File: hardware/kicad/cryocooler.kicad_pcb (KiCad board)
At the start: 4 copper layers, 130 x 100 mm, 208 parts, among them J1 USB_C, J10 RTD PT1000 4-wire, J11 AMP OUT (+ / -), J12 CRYOCOOLER (+ / -), J2 12V IN, J3 FAN (4-pin PWM), J4 PUMP (4-pin PWM), J5 ALPHACOOL ES FLOW (3-pin), J6 ALPHACOOL ES NTC 10k, J7 PANEL BUTTON, J8 AMP REM / GND, J9 AMP SIGNAL IN / GND, Q1 IRF4905S, Q2 BSS138, Q3 BSS138, Q4 BSS138, Q5 BSS138, Q6 BSS84, SW1 RESET, SW2 BOOT, SW3 POWER, U1 ESP32-S3-WROOM-2-N32R16V, U10 EMC2303-x-KP, U11 LTC2954CTS8-2, U12 LM4040DBZ-5, U13 CL25N8-G, U14 ADS122C04IPWR, U15 AP63205WU-7, U16 LD1117S33TR, U17 ISO7741DW, U18 ACS37800KMACTR-030B3-SPI, U19 LSM6DSOXTR, U2 USBLC6-2SC6, U20 ADP5071AREZ, U21 ADP7142AUJZ, U22 ADP7182AUJZ, U23 INA237AIDGSR, U24 74AHCT1G125, U3 SG-8002CA-PH 25MHz, U4 AD9833BRMZ, U5 OPA1656ID, U6 AD633JRZ-R7, U7 MCP4921-E/SN, U8 LM4040DBZ-2.5, U9 OPA188ID

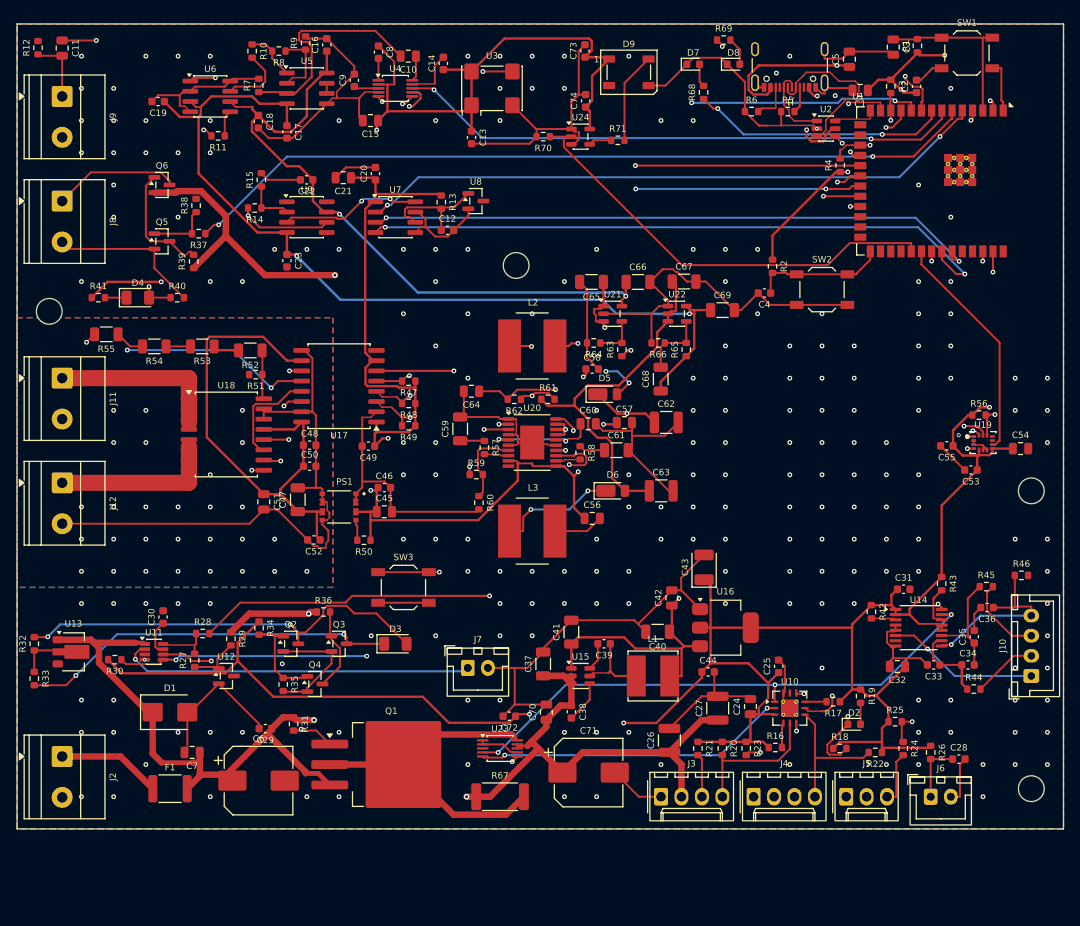
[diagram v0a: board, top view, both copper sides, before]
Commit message: KiCad PCB: regenerate and route for the new parts (DRC 0 errors, 0 unconnected)
- Places the INA239 LEDs and filter, the compressor relay driver, the
  SC18IS604 and its buffer, and about 40 test points; test points and the
  debug LEDs are placed beside a pad on their net.
- gen_pcb.py fixes: escape stubs now sample the whole stub and ignore only
  the pad's own tracks (diagonal-track bounding boxes hid real obstacles);
  isolated-side passives are derived from nets instead of fixed refs; ground
  pads boxed in by tracks get an escape via; locked 0.35 mm via-in-pad on the
  fine-pitch ground pads of U19, U23 and U4 before routing.
- tools/link_usb_vbus.py joins the USB-C VBUS pad pairs after routing.
- cryocooler.kicad_pro: net classes plus 0.35 mm via / 0.075 mm annular ring /
  0.2 mm drill limits for the via-in-pad (check the fab's minimums).

All 807 pad nets match the schematic netlist; only silkscreen warnings remain.

Co-Authored-By: Claude Sonnet 5.5 <noreply@anthropic.com>
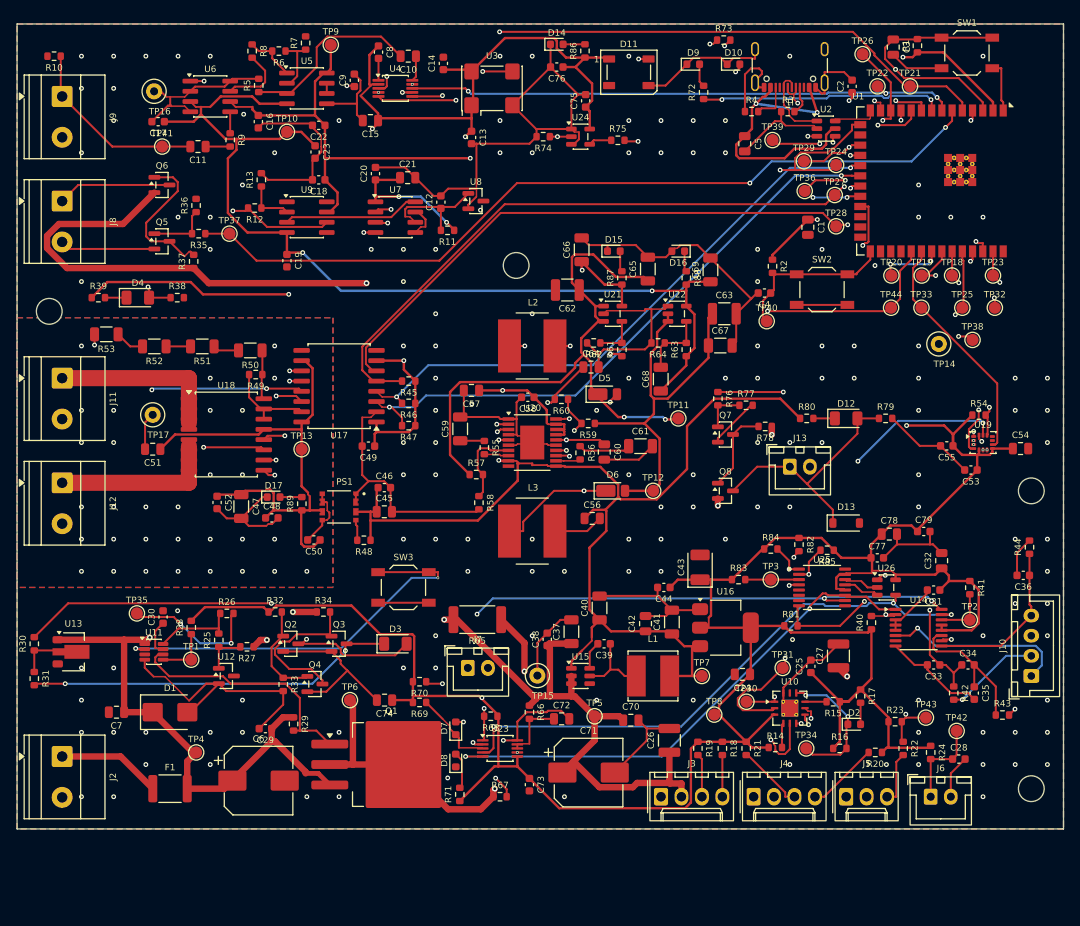
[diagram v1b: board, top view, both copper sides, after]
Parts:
- added C75: 100nF, C_0603_1608Metric, F.Cu at (70.6, 9.55)
- added C76: 100nF, C_0603_1608Metric, F.Cu at (67.0, 5.35)
- added C77: 100nF, C_0603_1608Metric, F.Cu at (106.9, 66.3)
- added C78: 1uF, C_0805_2012Metric, F.Cu at (108.4, 63.4)
- added C79: 100nF, C_0603_1608Metric, F.Cu at (112.6, 63.0)
- added D10: FAULT (red), LED_0603_1608Metric, F.Cu at (89.0, 5.00)
- added D11: WS2812B, LED_WS2812B_PLCC4_5.0x5.0mm_P3.2mm, F.Cu at (76.0, 6.00)
- added D12: RED/GREEN, LED_1206_3216Metric, F.Cu at (103.0, 49.0)
- added D13: 1N4148W, D_SOD-123, F.Cu at (103.0, 62.0)
- added D14: 5V (yellow), LED_0603_1608Metric, F.Cu at (67.0, 2.52)
- added D15: +15V (white), LED_0603_1608Metric, F.Cu at (74.1, 28.2)
- added D16: -15V (white), LED_0603_1608Metric, F.Cu at (82.1, 28.2)
- added D17: ISO 3V3 (green), LED_0603_1608Metric, F.Cu at (31.9, 58.8)
- added J13: COMPRESSOR RELAY / GND, JST_XH_B2B-XH-A_1x02_P2.50mm_Vertical, F.Cu at (96.0, 55.0)
- added Q7: BSS138, SOT-23, F.Cu at (88.0, 51.0)
- added Q8: BSS84, SOT-23, F.Cu at (88.0, 58.0)
- added R72: 470, R_0603_1608Metric, F.Cu at (85.3, 8.50)
- added R73: 470, R_0603_1608Metric, F.Cu at (87.8, 2.00)
- added R74: 10k, R_0603_1608Metric, F.Cu at (65.4, 14.0)
- added R75: 330, R_0603_1608Metric, F.Cu at (74.6, 14.4)
- added R76: 1k, R_0603_1608Metric, F.Cu at (87.1, 46.5)
- added R77: 100k, R_0603_1608Metric, F.Cu at (90.6, 47.4)
- added R78: 100k, R_0603_1608Metric, F.Cu at (92.9, 50.0)
- added R79: 1k, R_0603_1608Metric, F.Cu at (107.9, 49.0)
- added R80: 2.2k, R_0603_1608Metric, F.Cu at (98.1, 49.0)
- added R81: 10k, R_0603_1608Metric, F.Cu at (96.1, 74.8)
- added R82: 10k, R_0603_1608Metric, F.Cu at (97.1, 64.7)
- added R83: 10k, R_0603_1608Metric, F.Cu at (89.6, 69.0)
- added R84: 4.7k, R_0603_1608Metric, F.Cu at (93.6, 65.2)
- added R85: 4.7k, R_0603_1608Metric, F.Cu at (100.6, 65.4)
- added R86: 1k, R_0603_1608Metric, F.Cu at (70.5, 3.35)
- added R87: 4.7k, R_0603_1608Metric, F.Cu at (75.1, 31.6)
- added R88: 4.7k, R_0603_1608Metric, F.Cu at (83.1, 31.6)
- added R89: 1k, R_0603_1608Metric, F.Cu at (35.4, 59.6)
- added TP1: LTC2954_INT, TestPoint_Pad_D1.5mm, F.Cu at (21.6, 79.0)
- added TP10: -15V, TestPoint_Pad_D1.5mm, F.Cu at (33.5, 13.4)
- added TP11: +16V5, TestPoint_Pad_D1.5mm, F.Cu at (82.2, 49.0)
- added TP12: -16V5, TestPoint_Pad_D1.5mm, F.Cu at (79.0, 58.0)
- added TP13: ISO_3V3, TestPoint_Pad_D1.5mm, F.Cu at (35.4, 52.8)
- added TP14: GND, TestPoint_Loop_D2.50mm_Drill1.0mm, F.Cu at (114.5, 39.8)
- added TP15: GND, TestPoint_Loop_D2.50mm_Drill1.0mm, F.Cu at (64.6, 81.0)
- added TP16: GND, TestPoint_Loop_D2.50mm_Drill1.0mm, F.Cu at (17.0, 8.37)
- added TP17: ISO_GND, TestPoint_Loop_D2.50mm_Drill1.0mm, F.Cu at (16.9, 48.6)
- added TP18: SPI_SCK, TestPoint_Pad_D1.5mm, F.Cu at (116.2, 31.2)
- added TP19: SPI_MOSI, TestPoint_Pad_D1.5mm, F.Cu at (112.4, 31.2)
- added TP2: ADS1220_DRDY, TestPoint_Pad_D1.5mm, F.Cu at (118.4, 74.0)
- added TP20: SPI_MISO, TestPoint_Pad_D1.5mm, F.Cu at (108.6, 31.2)
- added TP21: MCP4921_CS, TestPoint_Pad_D1.5mm, F.Cu at (110.9, 7.75)
- added TP22: AD9833_FSYNC, TestPoint_Pad_D1.5mm, F.Cu at (106.9, 7.75)
- added TP23: IMU_CS, TestPoint_Pad_D1.5mm, F.Cu at (121.2, 31.2)
- added TP24: INA239_CS, TestPoint_Pad_D1.5mm, F.Cu at (101.8, 17.5)
- added TP25: ADS1220_CS, TestPoint_Pad_D1.5mm, F.Cu at (117.4, 35.2)
- added TP26: BRIDGE_CS, TestPoint_Pad_D1.5mm, F.Cu at (105.0, 3.75)
- added TP27: ACS_CS, TestPoint_Pad_D1.5mm, F.Cu at (101.6, 21.2)
- added TP28: ACS_MISO, TestPoint_Pad_D1.5mm, F.Cu at (101.8, 25.1)
- added TP29: BRIDGE_RESET, TestPoint_Pad_D1.5mm, F.Cu at (97.8, 17.1)
- added TP3: BRIDGE_INT, TestPoint_Pad_D1.5mm, F.Cu at (93.6, 69.0)
- added TP30: SDA, TestPoint_Pad_D1.5mm, F.Cu at (90.6, 84.2)
- added TP31: SCL, TestPoint_Pad_D1.5mm, F.Cu at (95.1, 80.0)
- added TP32: IMU_INT1, TestPoint_Pad_D1.5mm, F.Cu at (121.5, 35.2)
- added TP33: IMU_INT2, TestPoint_Pad_D1.5mm, F.Cu at (112.3, 35.2)
- added TP34: FAN_ALERT, TestPoint_Pad_D1.5mm, F.Cu at (98.0, 90.0)
- added TP35: PWR_KILL, TestPoint_Pad_D1.5mm, F.Cu at (14.9, 73.2)
- added TP36: COMP_RELAY_EN, TestPoint_Pad_D1.5mm, F.Cu at (97.8, 20.8)
- added TP37: AMP_REM_EN, TestPoint_Pad_D1.5mm, F.Cu at (26.4, 26.1)
- added TP38: UART0_TX, TestPoint_Pad_D1.5mm, F.Cu at (118.7, 39.2)
- added TP39: ESP_EN, TestPoint_Pad_D1.5mm, F.Cu at (93.8, 14.4)
- added TP4: VIN, TestPoint_Pad_D1.5mm, F.Cu at (22.2, 90.5)
- added TP40: ESP_BOOT, TestPoint_Pad_D1.5mm, F.Cu at (93.1, 36.9)
- added TP41: SIG_SINE, TestPoint_Pad_D1.5mm, F.Cu at (18.0, 15.2)
- added TP42: NTC_ADC, TestPoint_Pad_D1.5mm, F.Cu at (116.7, 87.8)
- added TP43: FLOW_TACH, TestPoint_Pad_D1.5mm, F.Cu at (112.9, 86.2)
- added TP44: STATUS_RGB, TestPoint_Pad_D1.5mm, F.Cu at (108.6, 35.2)
- added TP5: +12V, TestPoint_Pad_D1.5mm, F.Cu at (71.8, 86.0)
- added TP6: VSW, TestPoint_Pad_D1.5mm, F.Cu at (41.4, 84.0)
- added TP7: +5V, TestPoint_Pad_D1.5mm, F.Cu at (85.1, 81.0)
- added TP8: +3V3, TestPoint_Pad_D1.5mm, F.Cu at (86.6, 85.8)
- added TP9: +15V, TestPoint_Pad_D1.5mm, F.Cu at (39.0, 2.60)
- added U25: SC18IS604PW, TSSOP-16_4.4x5mm_P0.65mm, F.Cu at (100.0, 70.0)
- added U26: 74LVC1G125, SOT-23-5, F.Cu at (108.0, 70.0)
- C72: value 100nF -> 470nF; footprint C_0603_1608Metric -> C_0805_2012Metric
- C74: value 100nF -> 1uF; footprint C_0603_1608Metric -> C_0805_2012Metric
- D7: value READY (green) -> ALERT (red)
- D8: value FAULT (red) -> PWR (green)
- D9: value WS2812B -> READY (green); footprint LED_WS2812B_PLCC4_5.0x5.0mm_P3.2mm -> LED_0603_1608Metric
- R10: value 100 -> 100k
- R11: value 100 -> 6.8k
- R12: value 100k -> 30k
- R13: value 6.8k -> 10k
- R14: value 30k -> 33k
- R15: value 10k -> 4.7k
- R16: value 33k -> 10k
- R17: value 4.7k -> 1k
- R19: value 1k -> 4.7k
- R22, R42, R43, R70: value 10k -> 1k
- R23: value 4.7k -> 10k
- R24, R40, R45: value 1k -> 10k
- R25: value 10k -> 220k
- R27: value 220k -> 82k
- R29: value 82k -> 100k
- R3, R4: value 4.7k -> 5.1k
- R30: value 10k -> 330
- R31: value 100k -> 330
- R32: value 330 -> 10k
- R33: value 330 -> 100k
- R34, R48: value 10k -> 100k
- R35, R38: value 100k -> 1k
- R37: value 1k -> 100k
- R39: value 100k -> 2.2k
- R41: value 2.2k -> 10k
- R44: value 1k -> 3.9k
- R46: value 3.9k -> 10k
- R49: value 10k -> 4.02k
- R5: value 5.1k -> 100k
- R50: value 100k -> 1M; footprint R_0603_1608Metric -> R_1206_3216Metric
- R51: value 4.02k -> 1M; footprint R_0603_1608Metric -> R_1206_3216Metric
- R54: value 1M -> 10k; footprint R_1206_3216Metric -> R_0603_1608Metric
- R55: value 1M -> 5.6k; footprint R_1206_3216Metric -> R_0603_1608Metric
- R56: value 10k -> 12k
- R57: value 5.6k -> 2.67M
- R58: value 12k -> 137k
- R59: value 2.67M -> 2.55M
- R6: value 5.1k -> 51k
- R60: value 137k -> 118k
- R61: value 2.55M -> 115k
- R62: value 118k -> 10k
- R63: value 115k -> 113k
- R65: value 113k -> 15m; footprint R_0603_1608Metric -> R_2512_6332Metric
- R66: value 10k -> 49.9
- R67: value 15m -> 49.9; footprint R_2512_6332Metric -> R_0603_1608Metric
- R68, R69: value 470 -> 10k
- R7: value 100k -> 3.3k
- R71: value 330 -> 470
- R8: value 51k -> 100
- R9: value 3.3k -> 100
- U14: value ADS122C04IPWR -> ADS1220IPW
- U23: value INA237AIDGSR -> INA239AIDGSR
- moved R41 114.1 mm to (118.4, 70.0), turned to -90 degrees
- moved R54 102.8 mm to (119.5, 48.6), turned to 0 degrees
- moved R15 96.2 mm to (101.4, 84.2), turned to 180 degrees
- moved R40 95.2 mm to (106.1, 74.4), turned to 90 degrees
- moved R14 93.1 mm to (94.2, 89.9), turned to 0 degrees
- moved D8 93.1 mm to (54.5, 91.5), turned to 90 degrees
- moved C73 91.4 mm to (63.6, 94.5), turned to -90 degrees
- moved R69 90.5 mm to (50.0, 84.3), turned to 180 degrees
- moved R26 89.1 mm to (26.1, 73.2), turned to 0 degrees
- moved D7 87.6 mm to (54.5, 87.5), turned to 90 degrees
- moved R25 84.6 mm to (25.1, 76.5), turned to 90 degrees
- moved R71 83.6 mm to (55.0, 95.7), turned to 90 degrees
- moved R68 81.9 mm to (58.9, 86.0), turned to 180 degrees
- moved R46 79.1 mm to (48.6, 47.1), turned to 180 degrees
- moved C74 78.5 mm to (45.6, 84.0), turned to 180 degrees
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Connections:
- net /Amp Current/ISO_CS renamed Net-(U17-OUTC)
- net /Amp Current/ISO_MISO renamed Net-(U17-IND)
- net /Amp Current/ISO_MOSI renamed Net-(U17-OUTA)
- net /Amp Current/ISO_SCK renamed Net-(U17-OUTB)
- net Net-(U1-EN) renamed ESP_EN
- net Net-(U1-IO0) renamed ESP_BOOT
- C34 pad 2: Net-(U14-AIN0) -> Net-(U14-AIN0/REFP1)
- C35 pad 1: Net-(U14-AIN0) -> Net-(U14-AIN0/REFP1)
- C72 pad 1: +3V3 -> Net-(U23-IN-)
- C72 pad 2: GND -> Net-(U23-IN+)
- C73 pad 1: +5V -> +3V3
- C74 pad 1: +5V -> +3V3
- D7 pad 1: GND -> Net-(D7-K)
- D9 pad 1: +5V -> GND
- D9 pad 2: unconnected-(D9-DOUT-Pad2) -> Net-(D9-A)
- R10 pad 1: Net-(R10-Pad1) -> SIG_SINE
- R10 pad 2: Net-(U6-X1) -> GND
- R11 pad 1: Net-(U6-W) -> +3V3
- R11 pad 2: Net-(C11-Pad1) -> Net-(U7-Vref)
- R12 pad 1: SIG_SINE -> Net-(U9--)
- R12 pad 2: GND -> Net-(U6-Y1)
- R13 pad 1: +3V3 -> Net-(U9--)
- R13 pad 2: Net-(U7-Vref) -> GND
- R14 pad 1: Net-(U9--) -> +3V3
- R14 pad 2: Net-(U6-Y1) -> Net-(U10-ADDR_SEL)
- R15 pad 1: Net-(U9--) -> +3V3
- R15 pad 2: GND -> Net-(U10-CLK)
- R16 pad 2: Net-(U10-ADDR_SEL) -> FAN_ALERT
- R17 pad 2: Net-(U10-CLK) -> Net-(D2-A)
- R18 pad 2: FAN_ALERT -> Net-(J3-Pin_4)
- R19 pad 2: Net-(D2-A) -> Net-(J3-Pin_3)
- R20 pad 2: Net-(J3-Pin_4) -> Net-(J4-Pin_4)
- R21 pad 2: Net-(J3-Pin_3) -> Net-(J4-Pin_3)
- R22 pad 1: +3V3 -> FLOW_TACH
- R22 pad 2: Net-(J4-Pin_4) -> Net-(J5-Pin_3)
- R23 pad 2: Net-(J4-Pin_3) -> FLOW_TACH
- R24 pad 1: FLOW_TACH -> +3V3
- R24 pad 2: Net-(J5-Pin_3) -> NTC_ADC
- R25 pad 1: +3V3 -> Net-(U12-K)
- R25 pad 2: FLOW_TACH -> Net-(U11-~{KILL})
- R26 pad 1: +3V3 -> Net-(U11-~{KILL})
- R26 pad 2: NTC_ADC -> PWR_KILL
- R27 pad 1: Net-(U12-K) -> VIN
- R27 pad 2: Net-(U11-~{KILL}) -> Net-(U12-K)
- R28 pad 1: Net-(U11-~{KILL}) -> Net-(U11-~{INT})
- R28 pad 2: PWR_KILL -> +3V3
- R29 pad 2: Net-(U12-K) -> Net-(Q1-G)
- R3 pad 1: +3V3 -> GND
- R3 pad 2: SDA -> Net-(J1-CC1)
- R30 pad 1: PWR_INT -> Net-(U13-VB)
- R30 pad 2: +3V3 -> Net-(D3-AK)
- R31 pad 1: VIN -> Net-(U13-VB)
- R31 pad 2: Net-(Q1-G) -> Net-(D3-KA)
- R32 pad 1: Net-(U13-VB) -> +3V3
- R32 pad 2: Net-(D3-AK) -> Net-(Q2-G)
- R33 pad 1: Net-(U13-VB) -> Net-(Q2-G)
- R33 pad 2: Net-(D3-KA) -> GND
- R34 pad 1: +3V3 -> VIN
- R34 pad 2: Net-(Q2-G) -> Net-(Q3-G)
- R35 pad 1: Net-(Q2-G) -> AMP_REM_EN
- R35 pad 2: GND -> Net-(Q5-G)
- R36 pad 1: VIN -> Net-(Q5-G)
- R36 pad 2: Net-(Q3-G) -> GND
- R37 pad 1: AMP_REM_EN -> +12V
- R37 pad 2: Net-(Q5-G) -> Net-(Q5-D)
- R38 pad 1: Net-(Q5-G) -> /Amp Control/AMP_REM
- R39 pad 1: +12V -> +5V
- R39 pad 2: Net-(Q5-D) -> Net-(D4-KA)
- R4 pad 1: +3V3 -> GND
- R4 pad 2: SCL -> Net-(J1-CC2)
- R40 pad 1: /Amp Control/AMP_REM -> +3V3
- R40 pad 2: GND -> ADS1220_CS
- R41 pad 1: +5V -> +3V3
- R41 pad 2: Net-(D4-KA) -> Net-(U14-~{DRDY})
- R42 pad 1: +3V3 -> Net-(U14-AIN1)
- R42 pad 2: Net-(U14-~{RESET}) -> Net-(J10-Pin_2)
- R43 pad 1: +3V3 -> Net-(U14-AIN0/REFP1)
- R43 pad 2: Net-(U14-~{DRDY}) -> Net-(J10-Pin_3)
- R44 pad 1: Net-(U14-AIN1) -> Net-(J10-Pin_4)
- R44 pad 2: Net-(J10-Pin_2) -> GND
- R45 pad 1: Net-(U14-AIN0) -> +3V3
- R45 pad 2: Net-(J10-Pin_3) -> ACS_CS
- R46 pad 1: Net-(J10-Pin_4) -> +3V3
- R46 pad 2: GND -> ACS_SCK
- R47 pad 2: ACS_CS -> ACS_MOSI
- R48 pad 1: +3V3 -> +5V
- R48 pad 2: ACS_SCK -> Net-(PS1-EN)
- R49 pad 1: +3V3 -> Net-(U18-VINP)
- R49 pad 2: ACS_MOSI -> ISO_GND
- R5 pad 1: GND -> Net-(U5A-+)
- R5 pad 2: Net-(J1-CC1) -> GND
- R50 pad 1: +5V -> Net-(U18-VINP)
- R50 pad 2: Net-(PS1-EN) -> Net-(R50-Pad2)
- R51 pad 1: Net-(U18-VINP) -> Net-(R50-Pad2)
- R51 pad 2: ISO_GND -> Net-(R51-Pad2)
- R52 pad 1: Net-(U18-VINP) -> Net-(R51-Pad2)
- R53 pad 2: Net-(R53-Pad2) -> Net-(J12-Pin_1)
- R54 pad 1: Net-(R53-Pad2) -> +3V3
- R54 pad 2: Net-(R54-Pad2) -> IMU_CS
- R55 pad 1: Net-(R54-Pad2) -> Net-(C59-Pad1)
- R55 pad 2: Net-(J12-Pin_1) -> Net-(U20-COMP1)
- R56 pad 1: +3V3 -> Net-(C61-Pad1)
- R56 pad 2: IMU_CS -> Net-(U20-COMP2)
- R57 pad 1: Net-(C59-Pad1) -> +16V5
- R57 pad 2: Net-(U20-COMP1) -> Net-(U20-FB1)
- R58 pad 1: Net-(C61-Pad1) -> Net-(U20-FB1)
- R58 pad 2: Net-(U20-COMP2) -> GND
- R59 pad 1: +16V5 -> -16V5
- R59 pad 2: Net-(U20-FB1) -> Net-(U20-FB2)
- R6 pad 1: GND -> Net-(U5A--)
- R6 pad 2: Net-(J1-CC2) -> Net-(R6-Pad2)
- R60 pad 1: Net-(U20-FB1) -> Net-(U20-FB2)
- R60 pad 2: GND -> Net-(U20-VREF)
- R61 pad 1: -16V5 -> +15V
- R61 pad 2: Net-(U20-FB2) -> Net-(U21-SENSE/ADJ)
- R62 pad 1: Net-(U20-FB2) -> Net-(U21-SENSE/ADJ)
- R62 pad 2: Net-(U20-VREF) -> GND
- R63 pad 1: +15V -> -15V
- R63 pad 2: Net-(U21-SENSE/ADJ) -> Net-(U22-ADJ)
- R64 pad 1: Net-(U21-SENSE/ADJ) -> Net-(U22-ADJ)
- R65 pad 1: -15V -> VSW
- R65 pad 2: Net-(U22-ADJ) -> +12V
- R66 pad 1: Net-(U22-ADJ) -> +12V
- R66 pad 2: GND -> Net-(U23-IN-)
- R67 pad 1: +12V -> VSW
- R67 pad 2: VSW -> Net-(U23-IN+)
- R68 pad 1: LED_READY -> +3V3
- R68 pad 2: Net-(D7-A) -> INA239_CS
- R69 pad 1: LED_FAULT -> Net-(D7-K)
- R69 pad 2: Net-(D8-A) -> +3V3
- R7 pad 1: Net-(U5A-+) -> Net-(U5A--)
- R70 pad 1: STATUS_RGB -> Net-(D7-A)
- R70 pad 2: GND -> +3V3
- R71 pad 1: Net-(R71-Pad1) -> +3V3
- R71 pad 2: Net-(D9-DIN) -> Net-(D8-A)
- R8 pad 1: Net-(U5A--) -> Net-(R6-Pad2)
- R8 pad 2: Net-(R10-Pad1) -> Net-(U6-X1)
- R9 pad 1: Net-(U5A--) -> Net-(U6-W)
- R9 pad 2: GND -> Net-(C11-Pad1)
- U1 pad 12: SDA -> BRIDGE_CS
- U1 pad 15: unconnected-(U1-IO3-Pad15) -> INA239_CS
- U1 pad 17: SCL -> BRIDGE_RESET
- U1 pad 36: unconnected-(U1-RXD0-Pad36) -> ADS1220_CS
- U1 pad 37: unconnected-(U1-TXD0-Pad37) -> UART0_TX
- U1 pad 9: PWR_INT -> COMP_RELAY_EN
- U11 pad 5: PWR_INT -> Net-(U11-~{INT})
- U14 pad 1: +3V3 -> SPI_SCK
- U14 pad 11: Net-(U14-AIN0) -> Net-(U14-AIN0/REFP1)
- U14 pad 15: SDA -> SPI_MISO
- U14 pad 16: SCL -> SPI_MOSI
- U14 pad 2: +3V3 -> ADS1220_CS
- U14 pad 3: Net-(U14-~{RESET}) -> GND
- U23 pad 1: GND -> INA239_CS
- U23 pad 10: VSW -> Net-(U23-IN+)
- U23 pad 2: GND -> SPI_MOSI
- U23 pad 3: unconnected-(U23-~{Alert}-Pad3) -> Net-(D7-K)
- U23 pad 4: SDA -> SPI_MISO
- U23 pad 5: SCL -> SPI_SCK
- U23 pad 8: +12V -> Net-(U23-IN-)
- U23 pad 9: +12V -> Net-(U23-IN-)
- U24 pad 4: Net-(R71-Pad1) -> Net-(R75-Pad1)
- U5 pad 1: Net-(R10-Pad1) -> Net-(R6-Pad2)
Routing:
- net PWR_INT: track 156.6 -> 0.00 mm, vias 3 -> 0
- net SDA: track 136.6 -> 25.0 mm, vias 4 -> 2
- net INA239_CS: track 0.00 -> 105.1 mm, vias 0 -> 2
- net SPI_SCK: track 119.2 -> 222.6 mm, vias 4 -> 7
- net SPI_MISO: track 25.6 -> 128.5 mm, vias 2 -> 6
- net SCL: track 128.7 -> 30.7 mm, vias 4 -> 2
- net SPI_MOSI: track 119.7 -> 212.4 mm, vias 4 -> 8
- net BRIDGE_CS: track 0.00 -> 84.9 mm, vias 0 -> 3
- net +12V: track 194.9 -> 271.4 mm, vias 2 -> 5
- net BRIDGE_RESET: track 0.00 -> 69.2 mm, vias 0 -> 3
- net COMP_RELAY_EN: track 0.00 -> 63.8 mm, vias 0 -> 3
- net ADS1220_CS: track 0.00 -> 53.7 mm, vias 0 -> 2
- net +3V3: track 460.8 -> 512.5 mm
- net ISO_GND: track 73.1 -> 37.1 mm, vias 28 -> 31
- net +5V: track 278.8 -> 312.3 mm, vias 8 -> 5
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
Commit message: PCB silkscreen: button and LED labels, cryocooler logo, title and ALPHA mark
- Small labels beside the RESET / BOOT / POWER buttons, the panel button
  connector and every indicator LED (17 in all), each on the first side of
  the part that is clear of footprints, holes and reference texts.
- Back silkscreen: black-and-white trace of the Hybrid-98 cryocooler (stickers
  removed, vectorized with potrace, mirrored so it reads from the back) with
  "STI Hybrid-98 Cryocooler Control Unit" and "ALPHA DEV UNIT" below it,
  placed clear of the through-hole pads. Artwork and trace script are in
  hardware/kicad/artwork/.
- Front silkscreen: large "ALPHA" in the free spot nearest the board centre.
- Board re-routed from the generator: DRC 0 errors, 0 unconnected, and all 807
  pad nets still match the schematic.

Co-Authored-By: Claude Sonnet 5.5 <noreply@anthropic.com>
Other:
- board text added: "+15V"
- board text added: "-15V"
- board text added: "3V3"
- board text added: "5V"
- board text added: "ALERT"
- board text added: "ALPHA"
- board text added: "ALPHA DEV UNIT"
- board text added: "AMP REM"
- board text added: "BOOT"
- board text added: "COMP RLY"
- board text added: "FAN FAULT"
- board text added: "FAULT"
- board text added: "ISO 3V3"
- board text added: "PANEL BTN"
- board text added: "POWER"
- board text added: "READY"
- board text added: "RESET"
- board text added: "STATUS"
- board text added: "STI Hybrid-98 Cryocooler Control Unit"

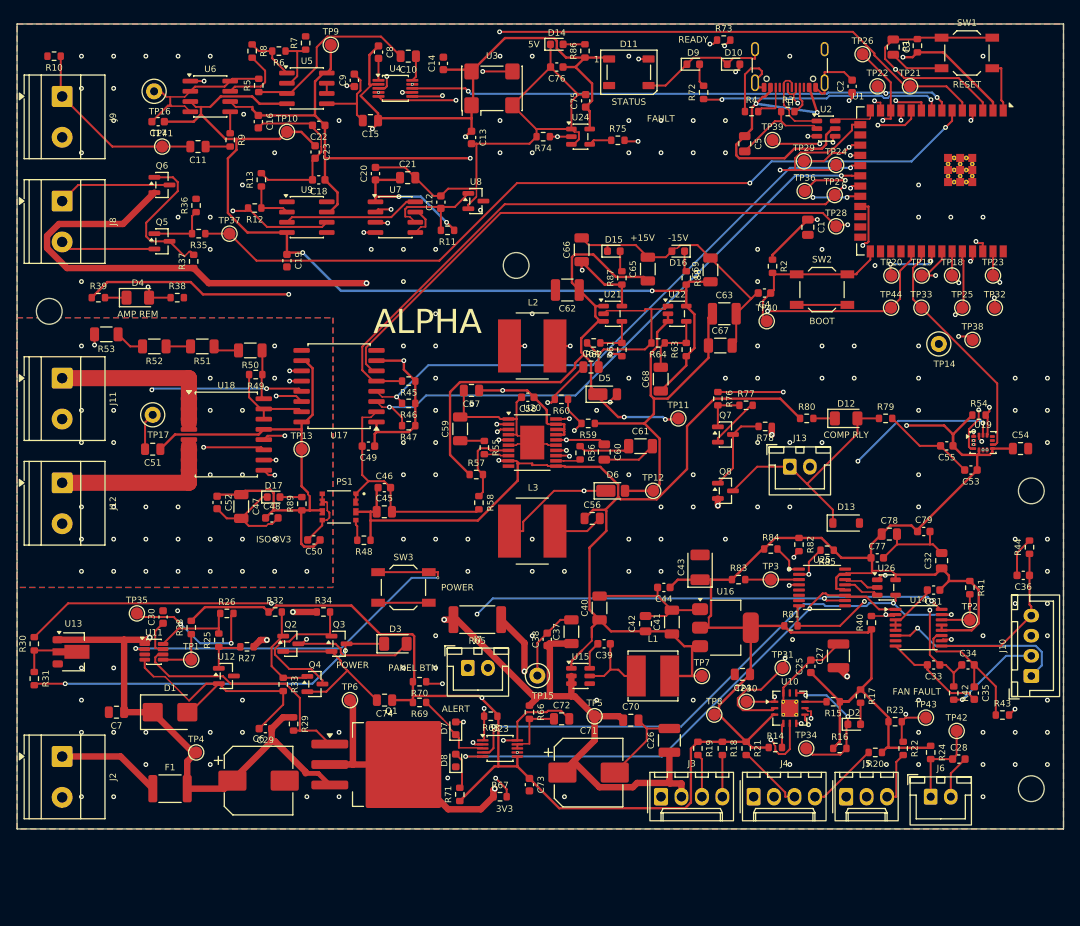
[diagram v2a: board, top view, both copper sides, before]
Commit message: Swap F1 to the Littelfuse NANO2 453 footprint and re-route
F1 is now the 5 A fast-acting Littelfuse 0453005.MR (2410 package); there is
no 5 A fast-acting fuse in 1812. Schematic, PCB (DRC 0 errors, 0 unconnected,
807/807 pad nets), Gerbers, BOM and notes regenerated.

Co-Authored-By: Claude Sonnet 5.5 <noreply@anthropic.com>
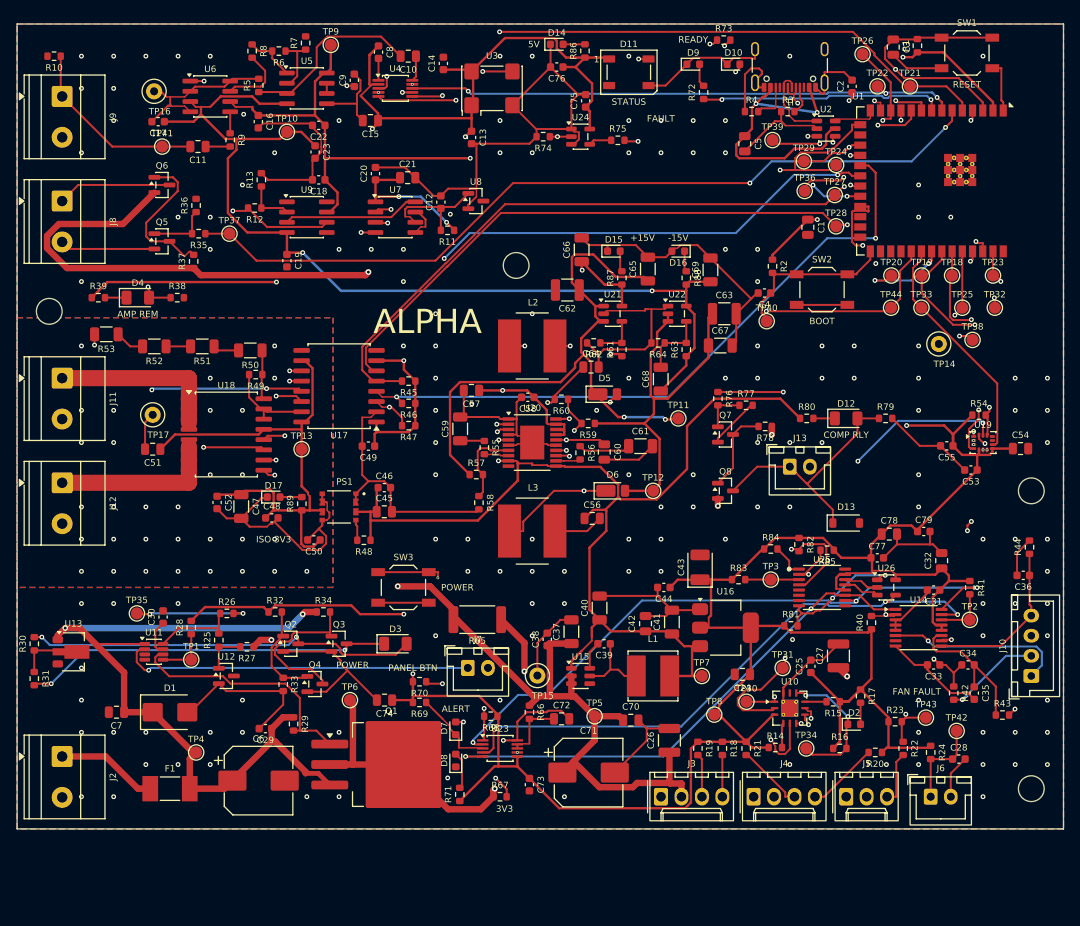
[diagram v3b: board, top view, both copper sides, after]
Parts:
- F1: footprint Fuse_1812_4532Metric -> Fuse_Littelfuse-NANO2-451_453
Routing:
- net SPI_MISO: track 128.5 -> 149.3 mm, vias 6 -> 8
- net +3V3: track 512.5 -> 491.7 mm, vias 8 -> 9
- net VIN: track 88.4 -> 105.3 mm
- net SPI_MOSI: track 212.4 -> 228.0 mm, vias 8 -> 7
- net GND: track 507.3 -> 494.5 mm
- net ISO_GND: track 37.1 -> 47.7 mm
- net ACS_SCK: track 73.4 -> 82.0 mm
- net Net-(U14-AIN1): track 18.6 -> 10.8 mm
- net UART0_TX: track 20.6 -> 13.0 mm
- net ACS_MOSI: track 75.4 -> 82.6 mm, vias 2 -> 3
- net Net-(D3-AK): track 55.1 -> 49.2 mm
- net BRIDGE_RESET: track 69.2 -> 73.6 mm, vias 3 -> 2
- net +12V: track 271.4 -> 274.4 mm
- net +5V: track 312.3 -> 309.3 mm
- net FAN_ALERT: track 82.9 -> 85.6 mm
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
